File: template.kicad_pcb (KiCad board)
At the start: 2 copper layers, 1 part

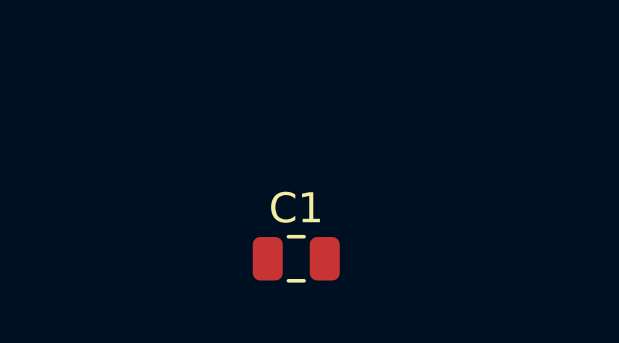
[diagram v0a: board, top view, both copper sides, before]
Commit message: added rules
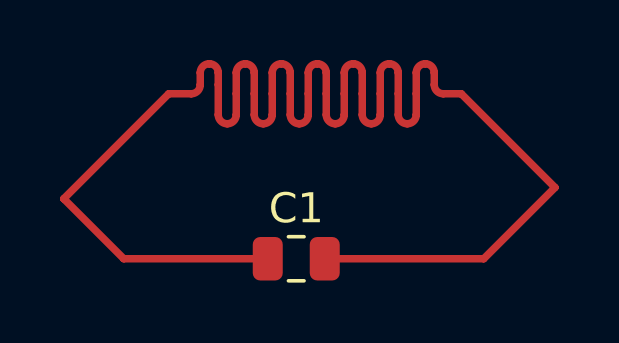
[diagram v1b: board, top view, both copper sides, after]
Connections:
- C1 pad 1: unconnected-(C1-Pad1) -> Net-(C1-Pad1)
- C1 pad 2: unconnected-(C1-Pad2) -> Net-(C1-Pad1)
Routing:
- net Net-(C1-Pad1): track 0.00 -> 57.5 mm
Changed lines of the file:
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@@
   )
   (setup
+    (stackup
+      (layer "F.SilkS" (type "Top Silk Screen"))
+      (layer "F.Paste" (type "Top Solder Paste"))
+      (layer "F.Mask" (type "Top Solder Mask") (thickness 0.01))
+      (layer "F.Cu" (type "copper") (thickness 0.035))
+      (layer "dielectric 1" (type "core") (thickness 1.51) (material "FR4") (epsilon_r 4.5) (loss_tangent 0.02))
+      (layer "B.Cu" (type "copper") (thickness 0.035))
+      (layer "B.Mask" (type "Bottom Solder Mask") (thickness 0.01))
+      (layer "B.Paste" (type "Bottom Solder Paste"))
+      (layer "B.SilkS" (type "Bottom Silk Screen"))
+      (copper_finish "None")
+      (dielectric_constraints no)
+    )
     (pad_to_mask_clearance 0)
     (pcbplotparams
@@
   )
   (net 0 "")
-  (net 1 "unconnected-(C1-Pad1)")
-  (net 2 "unconnected-(C1-Pad2)")
+  (net 1 "Net-(C1-Pad1)")
   (footprint "Capacitor_SMD:C_0805_2012Metric" (layer "F.Cu")
     (at 150.75 88.75)
@@
     (fp_line (start -1 -0.625) (end 1 -0.625) (layer "F.Fab") (width 0.1))
     (pad "1" smd roundrect (at -0.95 0) (size 1 1.45) (layers "F.Cu" "F.Paste" "F.Mask") (roundrect_rratio 0.25)
-      (net 1 "unconnected-(C1-Pad1)") (pintype "passive"))
+      (net 1 "Net-(C1-Pad1)") (pintype "passive"))
     (pad "2" smd roundrect (at 0.95 0) (size 1 1.45) (layers "F.Cu" "F.Paste" "F.Mask") (roundrect_rratio 0.25)
-      (net 2 "unconnected-(C1-Pad2)") (pintype "passive"))
+      (net 1 "Net-(C1-Pad1)") (pintype "passive"))
     (model "${KICAD6_3DMODEL_DIR}/Capacitor_SMD.3dshapes/C_0805_2012Metric.wrl"
       (offset (xyz 0 0 0))
@@
     )
   )
+  (segment (start 143 86.75) (end 146.5 83.25) (width 0.25) (layer "F.Cu") (net 1))
+  (segment (start 146.5 83.25) (end 147.25 83.25) (width 0.25) (layer "F.Cu") (net 1))
+  (segment (start 156.25 83.25) (end 159.375 86.375) (width 0.25) (layer "F.Cu") (net 1))
+  (segment (start 151.15 83.95) (end 151.15 83.25) (width 0.25) (layer "F.Cu") (net 1))
+  (segment (start 148.75 83.95) (end 148.75 83.25) (width 0.25) (layer "F.Cu") (net 1))
+  (segment (start 145 88.75) (end 143 86.75) (width 0.25) (layer "F.Cu") (net 1))
+  (segment (start 149.8 88.75) (end 145 88.75) (width 0.25) (layer "F.Cu") (net 1))
+  (segment (start 150.55 83.25) (end 150.55 83.95) (width 0.25) (layer "F.Cu") (net 1))
+  (segment (start 159.375 86.375) (end 157 88.75) (width 0.25) (layer "F.Cu") (net 1))
+  (segment (start 154.15 82.55) (end 154.15 83.25) (width 0.25) (layer "F.Cu") (net 1))
+  (segment (start 155.35 82.55) (end 155.35 82.95) (width 0.25) (layer "F.Cu") (net 1))
+  (segment (start 148.75 83.25) (end 148.75 82.55) (width 0.25) (layer "F.Cu") (net 1))
+  (segment (start 149.95 83.95) (end 149.95 83.25) (width 0.25) (layer "F.Cu") (net 1))
+  (segment (start 149.35 82.55) (end 149.35 83.25) (width 0.25) (layer "F.Cu") (net 1))
+  (segment (start 151.75 82.55) (end 151.75 83.25) (width 0.25) (layer "F.Cu") (net 1))
+  (segment (start 152.95 83.25) (end 152.95 83.95) (width 0.25) (layer "F.Cu") (net 1))
+  (segment (start 150.55 82.55) (end 150.55 83.25) (width 0.25) (layer "F.Cu") (net 1))
+  (segment (start 148.15 82.55) (end 148.15 82.95) (width 0.25) (layer "F.Cu") (net 1))
+  (segment (start 153.55 83.25) (end 153.55 82.55) (width 0.25) (layer "F.Cu") (net 1))
+  (segment (start 154.75 83.95) (end 154.75 83.25) (width 0.25) (layer "F.Cu") (net 1))
+  (segment (start 152.95 82.55) (end 152.95 83.25) (width 0.25) (layer "F.Cu") (net 1))
+  (segment (start 155.65 83.25) (end 156.25 83.25) (width 0.25) (layer "F.Cu") (net 1))
+  (segment (start 148.15 82.95) (end 148.15 83.95) (width 0.25) (layer "F.Cu") (net 1))
+  (segment (start 151.15 83.25) (end 151.15 82.55) (width 0.25) (layer "F.Cu") (net 1))
+  (segment (start 149.95 83.25) (end 149.95 82.55) (width 0.25) (layer "F.Cu") (net 1))
+  (segment (start 147.55 82.95) (end 147.55 82.55) (width 0.25) (layer "F.Cu") (net 1))
+  (segment (start 152.35 83.25) (end 152.35 82.55) (width 0.25) (layer "F.Cu") (net 1))
+  (segment (start 149.35 83.25) (end 149.35 83.95) (width 0.25) (layer "F.Cu") (net 1))
+  (segment (start 154.75 83.25) (end 154.75 82.55) (width 0.25) (layer "F.Cu") (net 1))
+  (segment (start 153.55 83.95) (end 153.55 83.25) (width 0.25) (layer "F.Cu") (net 1))
+  (segment (start 154.15 83.25) (end 154.15 83.95) (width 0.25) (layer "F.Cu") (net 1))
+  (segment (start 157 88.75) (end 151.7 88.75) (width 0.25) (layer "F.Cu") (net 1))
+  (segment (start 152.35 83.95) (end 152.35 83.25) (width 0.25) (layer "F.Cu") (net 1))
+  (segment (start 151.75 83.25) (end 151.75 83.95) (width 0.25) (layer "F.Cu") (net 1))
+  (arc (start 150.55 83.95) (mid 150.637868 84.162132) (end 150.85 84.25) (width 0.25) (layer "F.Cu") (net 1))
+  (arc (start 153.85 82.25) (mid 154.062132 82.337868) (end 154.15 82.55) (width 0.25) (layer "F.Cu") (net 1))
+  (arc (start 152.35 82.55) (mid 152.437868 82.337868) (end 152.65 82.25) (width 0.25) (layer "F.Cu") (net 1))
+  (arc (start 149.95 82.55) (mid 150.037868 82.337868) (end 150.25 82.25) (width 0.25) (layer "F.Cu") (net 1))
+  (arc (start 152.65 82.25) (mid 152.862132 82.337868) (end 152.95 82.55) (width 0.25) (layer "F.Cu") (net 1))
+  (arc (start 148.45 84.25) (mid 148.662132 84.162132) (end 148.75 83.95) (width 0.25) (layer "F.Cu") (net 1))
+  (arc (start 154.75 82.55) (mid 154.837868 82.337868) (end 155.05 82.25) (width 0.25) (layer "F.Cu") (net 1))
+  (arc (start 151.45 82.25) (mid 151.662132 82.337868) (end 151.75 82.55) (width 0.25) (layer "F.Cu") (net 1))
+  (arc (start 151.15 82.55) (mid 151.237868 82.337868) (end 151.45 82.25) (width 0.25) (layer "F.Cu") (net 1))
+  (arc (start 154.15 83.95) (mid 154.237868 84.162132) (end 154.45 84.25) (width 0.25) (layer "F.Cu") (net 1))
+  (arc (start 148.75 82.55) (mid 148.837868 82.337868) (end 149.05 82.25) (width 0.25) (layer "F.Cu") (net 1))
+  (arc (start 147.55 82.55) (mid 147.637868 82.337868) (end 147.85 82.25) (width 0.25) (layer "F.Cu") (net 1))
+  (arc (start 147.85 82.25) (mid 148.062132 82.337868) (end 148.15 82.55) (width 0.25) (layer "F.Cu") (net 1))
+  (arc (start 150.25 82.25) (mid 150.462132 82.337868) (end 150.55 82.55) (width 0.25) (layer "F.Cu") (net 1))
+  (arc (start 152.95 83.95) (mid 153.037868 84.162132) (end 153.25 84.25) (width 0.25) (layer "F.Cu") (net 1))
+  (arc (start 155.35 82.95) (mid 155.437868 83.162132) (end 155.65 83.25) (width 0.25) (layer "F.Cu") (net 1))
+  (arc (start 153.55 82.55) (mid 153.637868 82.337868) (end 153.85 82.25) (width 0.25) (layer "F.Cu") (net 1))
+  (arc (start 149.65 84.25) (mid 149.862132 84.162132) (end 149.95 83.95) (width 0.25) (layer "F.Cu") (net 1))
+  (arc (start 151.75 83.95) (mid 151.837868 84.162132) (end 152.05 84.25) (width 0.25) (layer "F.Cu") (net 1))
+  (arc (start 150.85 84.25) (mid 151.062132 84.162132) (end 151.15 83.95) (width 0.25) (layer "F.Cu") (net 1))
+  (arc (start 153.25 84.25) (mid 153.462132 84.162132) (end 153.55 83.95) (width 0.25) (layer "F.Cu") (net 1))
+  (arc (start 149.35 83.95) (mid 149.437868 84.162132) (end 149.65 84.25) (width 0.25) (layer "F.Cu") (net 1))
+  (arc (start 148.15 83.95) (mid 148.237868 84.162132) (end 148.45 84.25) (width 0.25) (layer "F.Cu") (net 1))
+  (arc (start 147.25 83.25) (mid 147.462132 83.162132) (end 147.55 82.95) (width 0.25) (layer "F.Cu") (net 1))
+  (arc (start 152.05 84.25) (mid 152.262132 84.162132) (end 152.35 83.95) (width 0.25) (layer "F.Cu") (net 1))
+  (arc (start 154.45 84.25) (mid 154.662132 84.162132) (end 154.75 83.95) (width 0.25) (layer "F.Cu") (net 1))
+  (arc (start 155.05 82.25) (mid 155.262132 82.337868) (end 155.35 82.55) (width 0.25) (layer "F.Cu") (net 1))
+  (arc (start 149.05 82.25) (mid 149.262132 82.337868) (end 149.35 82.55) (width 0.25) (layer "F.Cu") (net 1))
 )
